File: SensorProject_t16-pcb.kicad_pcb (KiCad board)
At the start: 2 copper layers, 48.3 x 71.1 mm, 92 parts, among them J1 Conn_01x02_Pin, J10 Conn_01x02_Pin, J11 Conn_01x02_Pin, J12 Conn_01x02_Pin, J13 Conn_01x02_Pin, J14 Conn_01x02_Pin, J15 Conn_01x02_Pin, J16 Conn_01x02_Pin, J18 Conn_02x04_Top_Bottom, J2 Conn_01x02_Pin, J20 Screw_Terminal_01x02, J3 Conn_01x02_Pin, J4 Conn_01x02_Pin, J5 Conn_01x02_Pin, J6 Conn_01x02_Pin, J7 Conn_01x02_Pin, J8 Conn_01x02_Pin, J9 Conn_01x02_Pin, SW1 SW_Push, SW2 SW_Push, U1 ADS1115IDGS, U2 ADS1115IDGS, U3 ADS1115IDGS, U4 ADS1115IDGS, U5 STM32F411CEU6, U6 AMS1117-3.3 SOT-223, U7 RFM95W-915S2, Y1 25MHz, Y2 32.758kHz

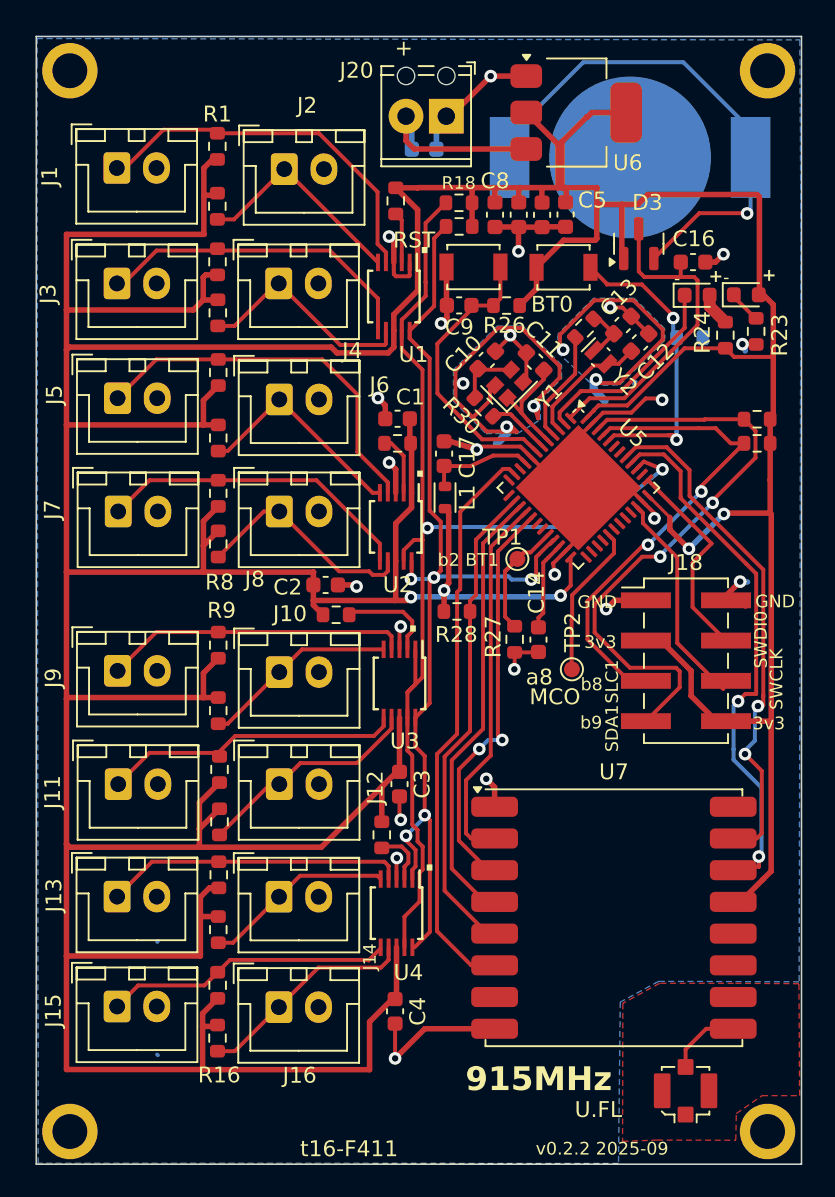
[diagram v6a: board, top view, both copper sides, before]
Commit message: finished flipping radio side.
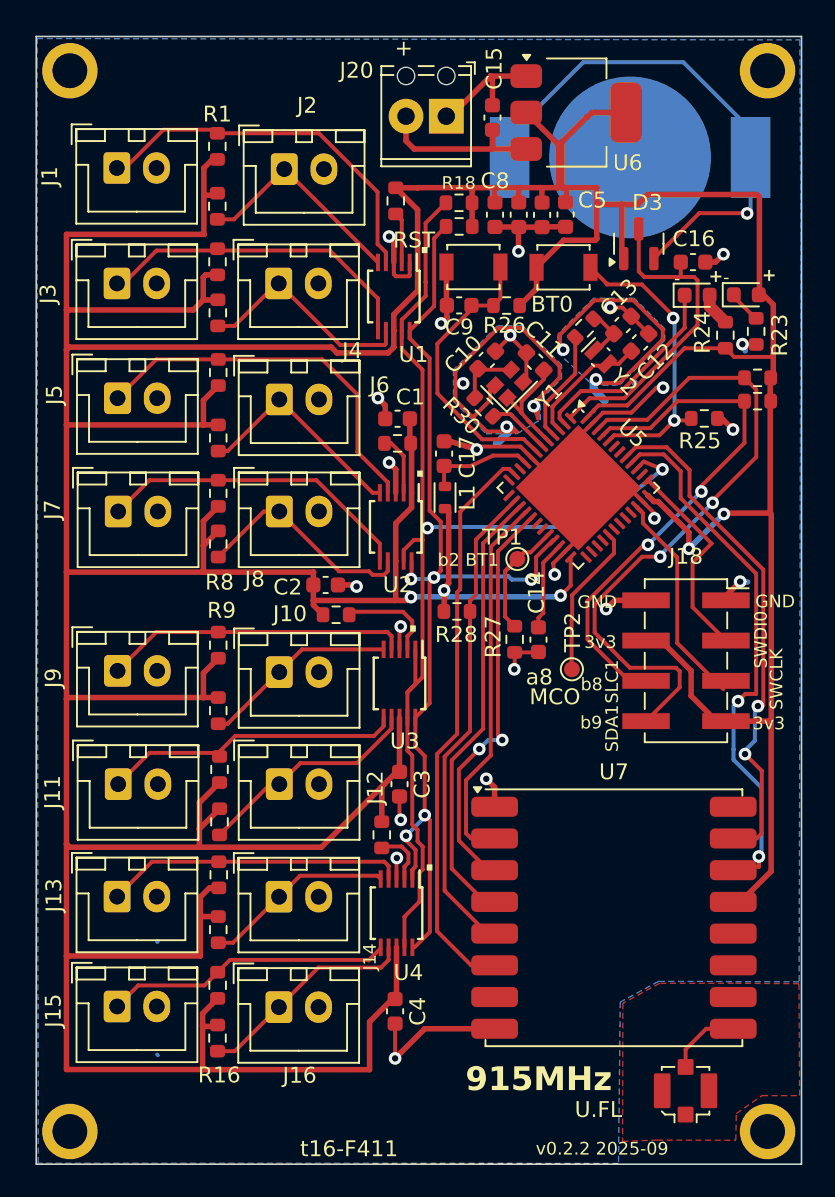
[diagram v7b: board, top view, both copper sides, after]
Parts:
- C15, R25: moved to F.Cu
- J18: footprint ProjectLib:PinHeader_2x04_P2.54mm_Vertical_SMD -> ProjectLib:PinSocket_2x04_P2.54mm_Vertical_SMD
- moved R25 5.17 mm to (91.7, 48.2)
- moved C15 4.75 mm to (78.3, 29.2), turned to 90 degrees
- moved R33 2.66 mm to (95.0, 47.1)
- moved R34 2.61 mm to (95.0, 45.7)
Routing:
- net SDA1: track 38.5 -> 42.3 mm
- net SCL1: track 30.9 -> 32.8 mm
- net GND: track 73.4 -> 75.1 mm
- net DIO0: track 35.4 -> 33.9 mm
- net Net-(U5-BOOT0): track 20.2 -> 19.0 mm
- net SCK: track 28.2 -> 27.6 mm

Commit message: converted R, C, and L to smaller 0402 footprints. Some trace rearranging and cleanup.
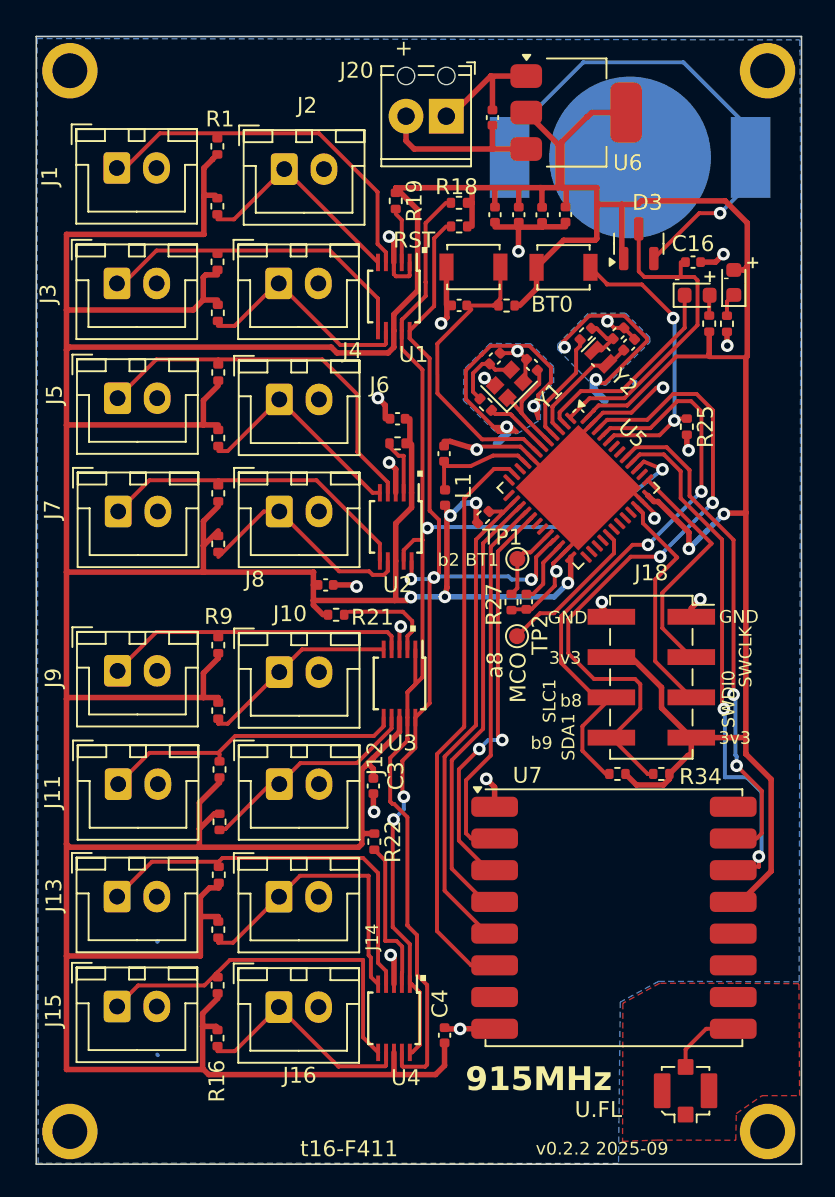
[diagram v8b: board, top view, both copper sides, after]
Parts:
- C1, C10, C11, C12, C13, C14, C15, C16, C17, C2, C3, C4, C5, C6, C7, C8, C9: footprint ProjectLib:C_0603_1608Metric -> ProjectLib:C_0402_1005Metric
- L1: footprint ProjectLib:L_TDK_MLZ1608 -> ProjectLib:L_0402_1005Metric
- R1, R10, R11, R12, R13, R14, R15, R16, R17, R18, R19, R2, R20, R21, R22, R23, R24, R25, R26, R27, R28, R29, R3, R30, R33, R34, R4, R5, R6, R7, R8, R9: footprint ProjectLib:R_0603_1608Metric -> ProjectLib:R_0402_1005Metric
- moved R34 25.7 mm to (89.0, 70.6)
- moved R33 25.1 mm to (86.2, 70.6)
- moved U4 6.63 mm to (72.1, 86.0)
- moved R28 6.17 mm to (77.7, 54.5), turned to 45 degrees
- moved TP2 4.04 mm to (79.8, 62.0)
- moved C4 3.47 mm to (75.3, 87.1), turned to 90 degrees
- moved C14 2.51 mm to (80.4, 59.8)
- moved J18 2.42 mm to (88.3, 64.5)
- moved R27 2.36 mm to (79.5, 59.8)
- moved R23 1.90 mm to (93.1, 42.2)
- moved C3 1.65 mm to (70.8, 71.4)
- moved R24 1.25 mm to (92.0, 42.2)
- moved R25 1.22 mm to (90.6, 48.7), turned to -90 degrees
- moved D1 1.11 mm to (93.5, 39.6), turned to 90 degrees
- moved C12 0.70 mm to (86.9, 43.6)
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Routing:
- net SDA2: track 73.0 -> 83.6 mm
- net +3V3: track 418.6 -> 428.0 mm, vias 5 -> 7
- net GND: track 75.1 -> 68.2 mm, vias 21 -> 20
- net Net-(J14-Pin_1): track 12.1 -> 18.6 mm
- net Net-(U4-ALERT/RDY): track 3.50 -> 9.63 mm
- net Net-(J13-Pin_1): track 19.0 -> 25.1 mm
- net GND_HSE: track 29.4 -> 23.4 mm
- net Net-(J15-Pin_1): track 18.2 -> 23.1 mm
- net GND_LSE: track 19.7 -> 15.0 mm
- net SCL1: track 32.8 -> 36.9 mm
- net Net-(U5-PB2): track 8.53 -> 4.95 mm
- net SCL2: track 65.2 -> 68.3 mm
- net Net-(BT1-+): track 29.6 -> 27.0 mm
- net /f411/SWCLK: track 13.2 -> 14.9 mm
- net Net-(U5-VCAP1): track 5.69 -> 4.15 mm
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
